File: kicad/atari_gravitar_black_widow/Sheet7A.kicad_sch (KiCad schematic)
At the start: 29 parts

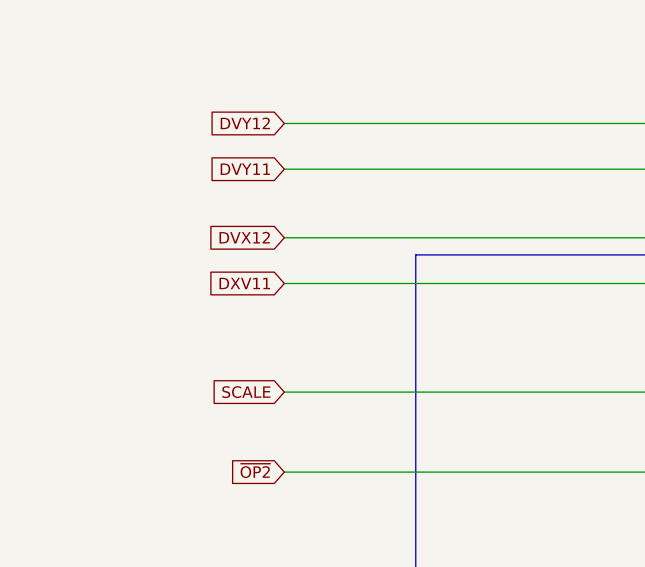
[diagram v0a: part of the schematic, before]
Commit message: Removed more warnings - 25 warnings remain
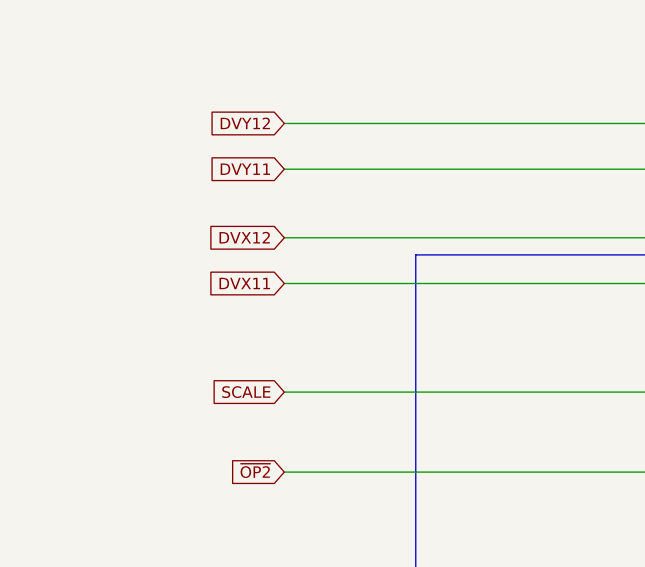
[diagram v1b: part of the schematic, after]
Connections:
- net DXV11 renamed DVX11
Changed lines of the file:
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@@
     )
   )
-  (global_label "DXV11" (shape input) (at 50.165 85.09 180) (fields_autoplaced)
+  (global_label "DVX11" (shape input) (at 50.165 85.09 180) (fields_autoplaced)
     (effects (font (size 1.27 1.27)) (justify right))
-    (property "Intersheet References" "${INTERSHEET_REFS}" (id 0) (at 0 0 0)
-      (effects (font (size 1.27 1.27)) hide)
+    (property "Intersheet References" "${INTERSHEET_REFS}" (id 0) (at 41.8537 85.0106 0)
+      (effects (font (size 1.27 1.27)) (justify right) hide)
     )
   )

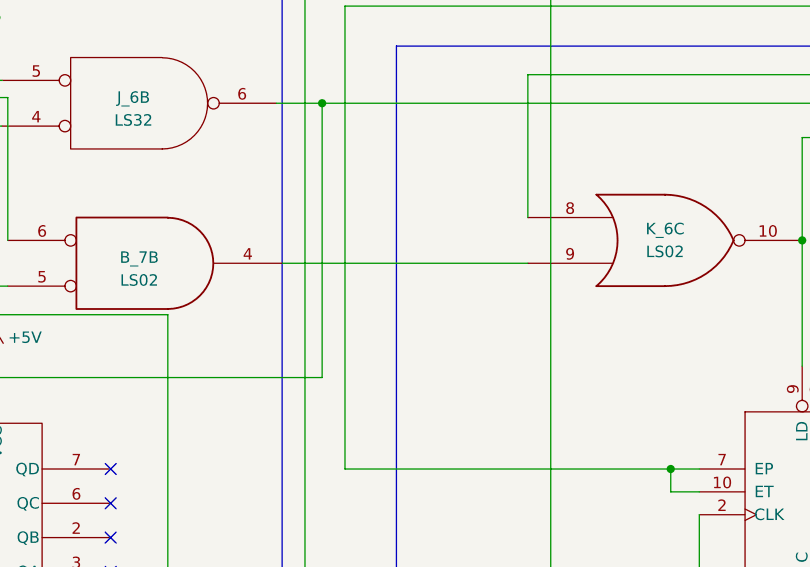
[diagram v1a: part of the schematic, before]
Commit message: 20 warnings left kicad 6.0
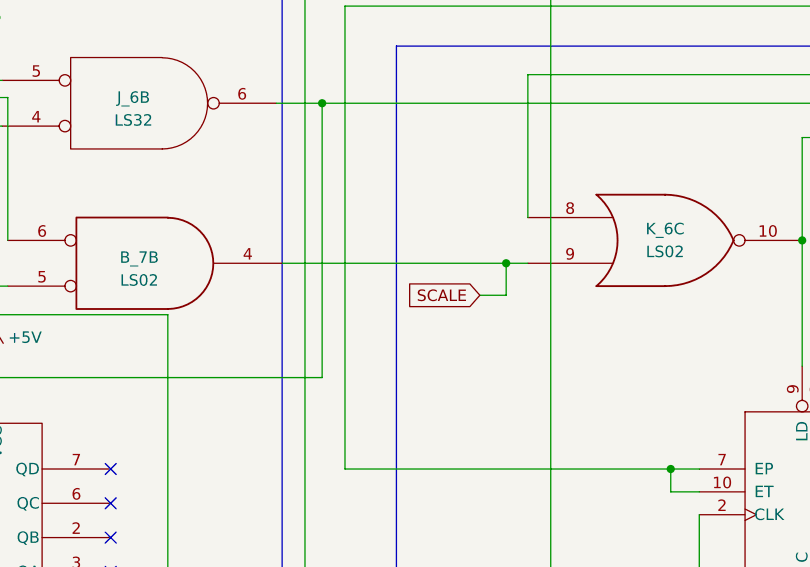
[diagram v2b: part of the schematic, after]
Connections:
- net SCALE: now also B_7.4, K_6.9
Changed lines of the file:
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@@
   (junction (at 361.315 255.905) (diameter 0) (color 0 0 0 0)
+  )
+  (junction (at 179.197 269.875) (diameter 0) (color 0 0 0 0)
   )
   (junction (at 401.32 295.275) (diameter 0) (color 0 0 0 0)
@@
     (stroke (width 0) (type default) (color 0 0 0 0))
   )
+  (wire (pts (xy 179.197 273.431) (xy 176.276 273.431))
+    (stroke (width 0) (type default) (color 0 0 0 0))
+  )
   (polyline (pts (xy 64.77 140.97) (xy 305.435 140.97))
     (stroke (width 0) (type default) (color 0 0 0 0))
@@
     (stroke (width 0) (type default) (color 0 0 0 0))
   )
-  (wire (pts (xy 154.305 269.875) (xy 181.61 269.875))
+  (wire (pts (xy 154.305 269.875) (xy 179.197 269.875))
     (stroke (width 0) (type default) (color 0 0 0 0))
   )
@@
     (stroke (width 0) (type default) (color 0 0 0 0))
   )
+  (wire (pts (xy 179.197 269.875) (xy 179.197 273.431))
+    (stroke (width 0) (type default) (color 0 0 0 0))
+  )
   (wire (pts (xy 361.315 255.905) (xy 361.315 281.305))
     (stroke (width 0) (type default) (color 0 0 0 0))
@@
   )
   (wire (pts (xy 461.645 205.105) (xy 461.645 254.635))
+    (stroke (width 0) (type default) (color 0 0 0 0))
+  )
+  (wire (pts (xy 179.197 269.875) (xy 181.61 269.875))
     (stroke (width 0) (type default) (color 0 0 0 0))
   )
@@
     )
   )
+  (global_label "SCALE" (shape input) (at 176.276 273.431 180) (fields_autoplaced)
+    (effects (font (size 1.27 1.27)) (justify right))
+    (property "Intersheet References" "${INTERSHEET_REFS}" (id 0) (at 168.2066 273.3516 0)
+      (effects (font (size 1.27 1.27)) (justify right) hide)
+    )
+  )

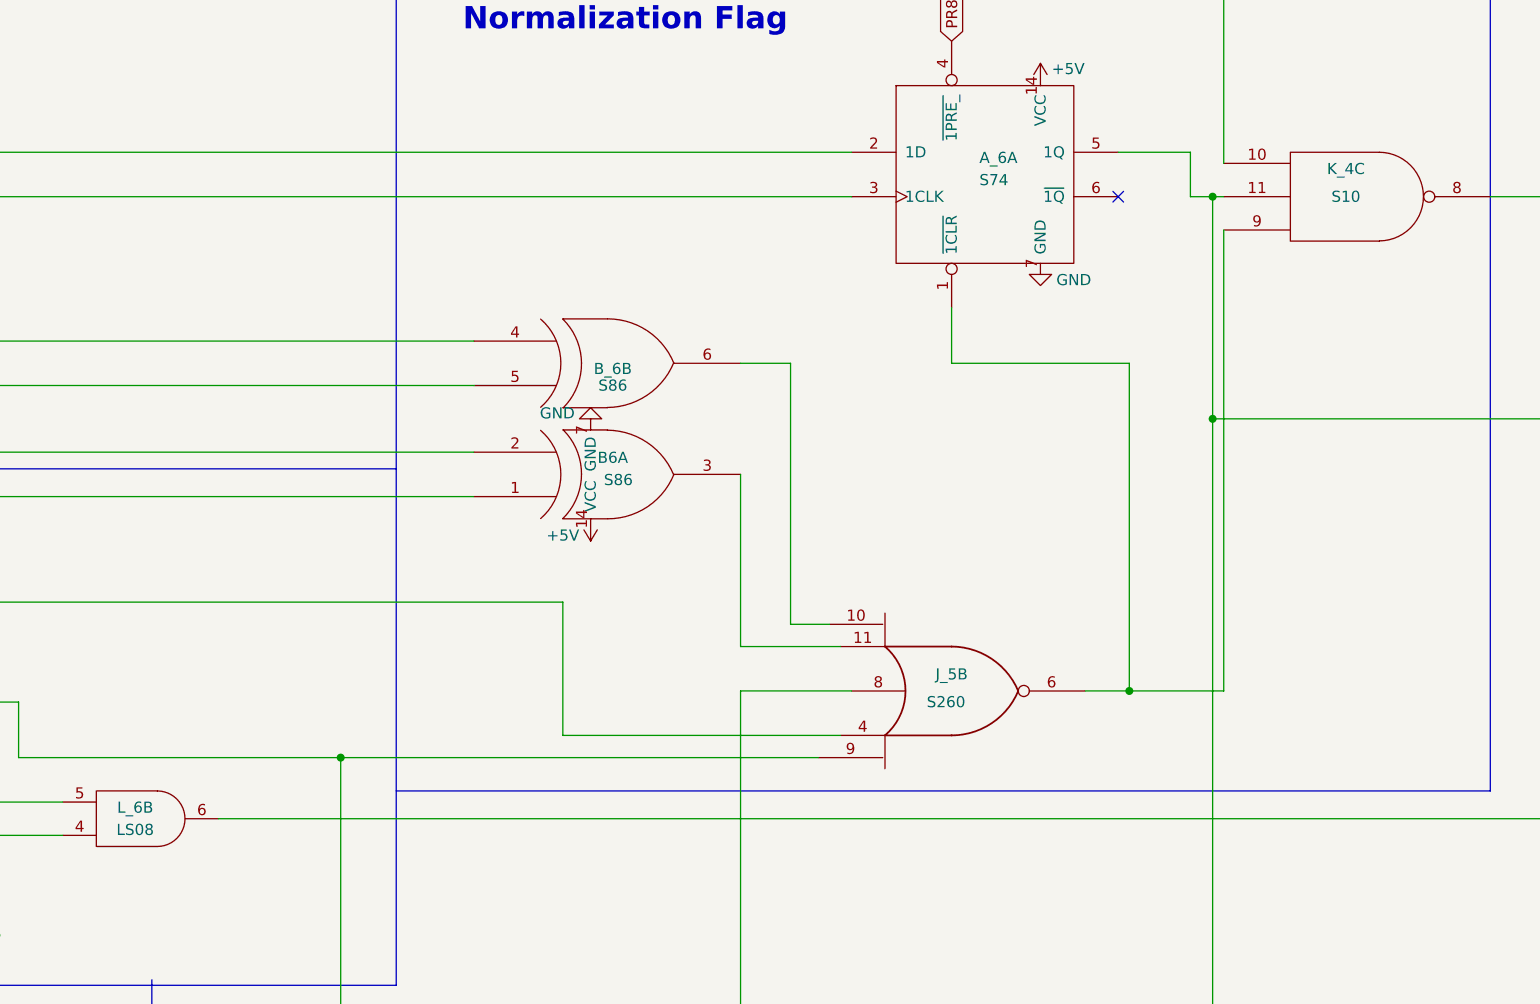
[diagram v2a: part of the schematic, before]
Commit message: Fixed all warnings and errors
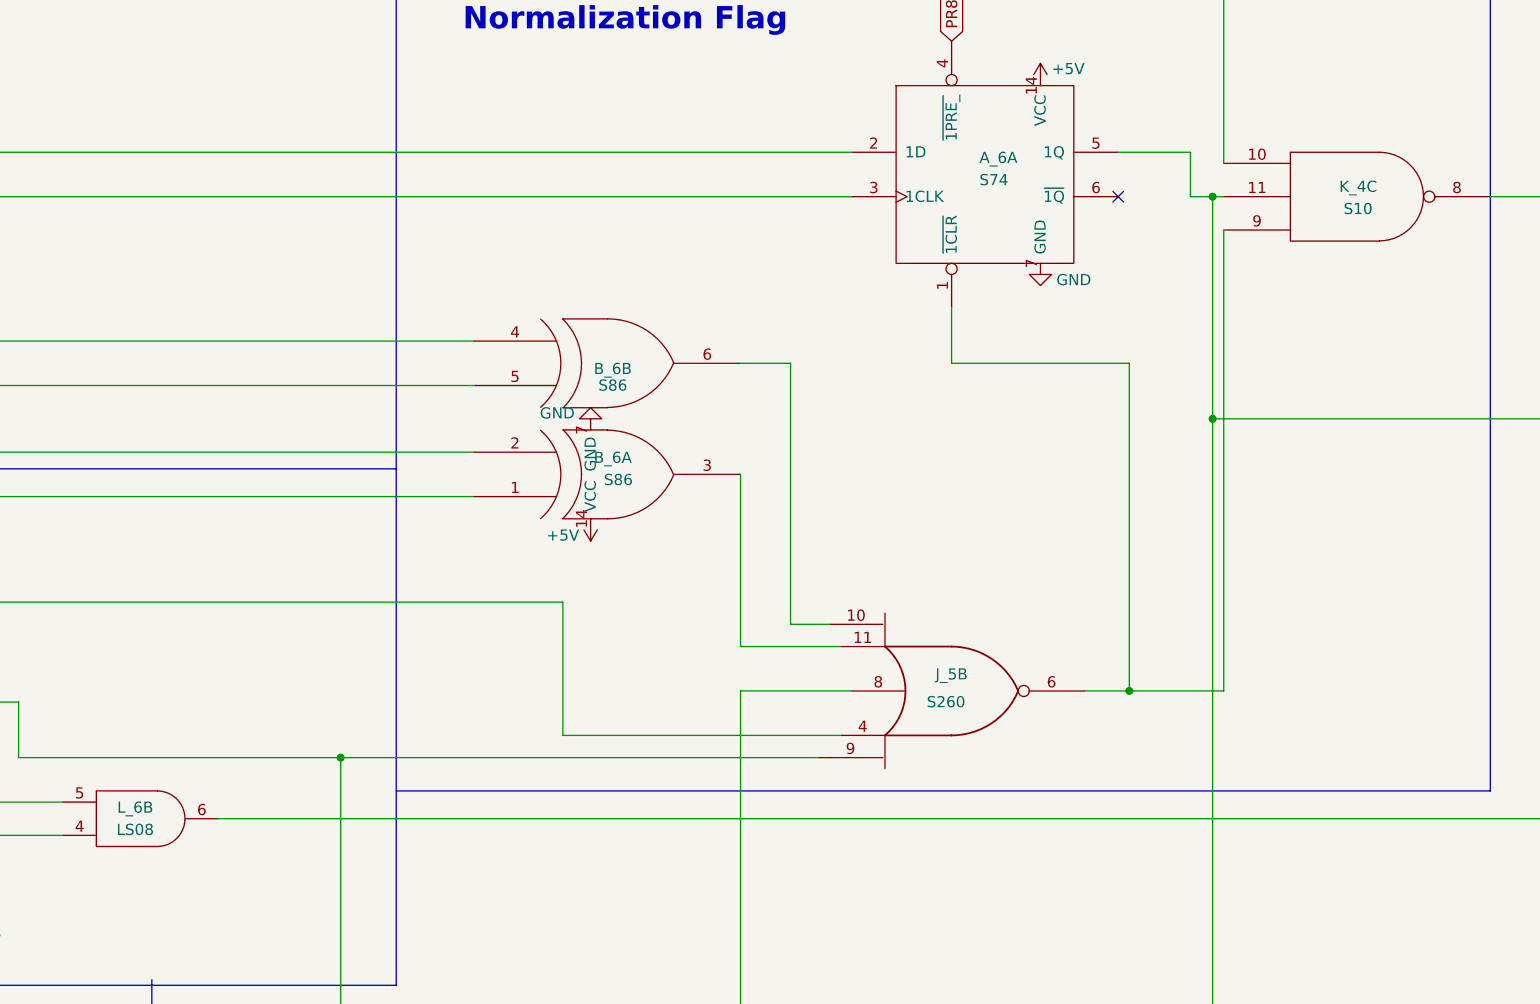
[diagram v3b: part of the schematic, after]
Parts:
- renumbered B6 to B_6
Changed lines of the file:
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@@
     (pin "6")
-  )
-  (symbol (lib_id "atari_grav_bw:LS10") (at 415.29 50.8 0) (unit 3)
-    (in_bom yes) (on_board yes)
-    (property "Reference" "K_4" (id 0) (at 414.02 47.625 0))
-    (property "Value" "S10" (id 1) (at 414.02 50.8 0))
-    (property "Footprint" "" (id 2) (at 415.29 50.8 0)
-      (effects (font (size 1.27 1.27)) hide)
-    )
-    (property "Datasheet" "" (id 3) (at 415.29 50.8 0)
-      (effects (font (size 1.27 1.27)) hide)
-    )
-    (pin "10")
-    (pin "11")
-    (pin "8")
-    (pin "9")
   )
   (symbol (lib_id "Star_Wars_Vector_PCB:LS08") (at 275.59 121.92 0) (mirror x) (unit 2)
@@
   (symbol (lib_id "Star_Wars_Vector_PCB:LS86") (at 329.565 82.55 0) (mirror x) (unit 1)
     (in_bom yes) (on_board yes)
-    (property "Reference" "B6" (id 0) (at 330.2 80.645 0))
+    (property "Reference" "B_6" (id 0) (at 330.2 80.645 0))
     (property "Value" "S86" (id 1) (at 330.835 83.185 0))
     (property "Footprint" "" (id 2) (at 329.565 82.55 0)
@@
     (pin "1")
   )
+  (symbol (lib_id "atari_grav_bw:LS10") (at 415.29 50.8 0) (unit 3)
+    (in_bom yes) (on_board yes)
+    (property "Reference" "K_4" (id 0) (at 415.417 49.657 0))
+    (property "Value" "S10" (id 1) (at 415.417 52.197 0))
+    (property "Footprint" "" (id 2) (at 415.29 50.8 0)
+      (effects (font (size 1.27 1.27)) hide)
+    )
+    (property "Datasheet" "" (id 3) (at 415.29 50.8 0)
+      (effects (font (size 1.27 1.27)) hide)
+    )
+    (pin "10")
+    (pin "11")
+    (pin "8")
+    (pin "9")
+  )
   (symbol (lib_id "power:+5V") (at 234.315 156.21 0) (unit 1)

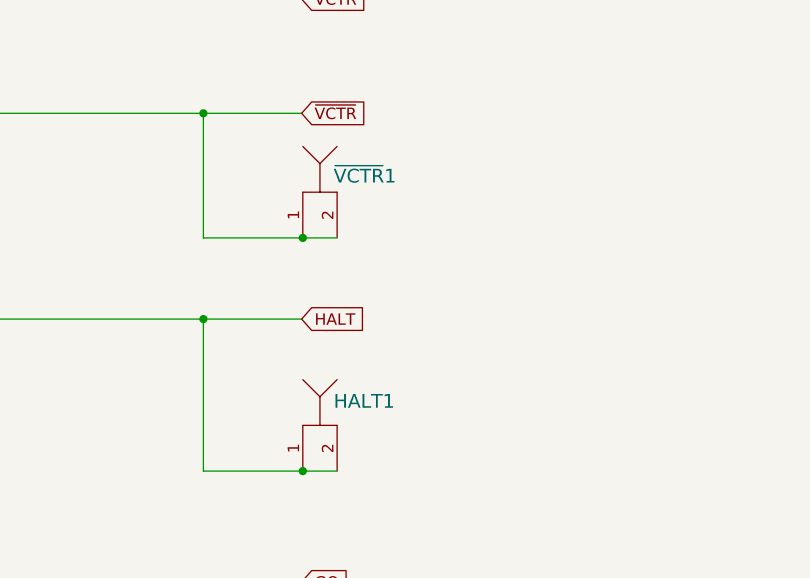
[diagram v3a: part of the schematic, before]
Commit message: Added PCB outline
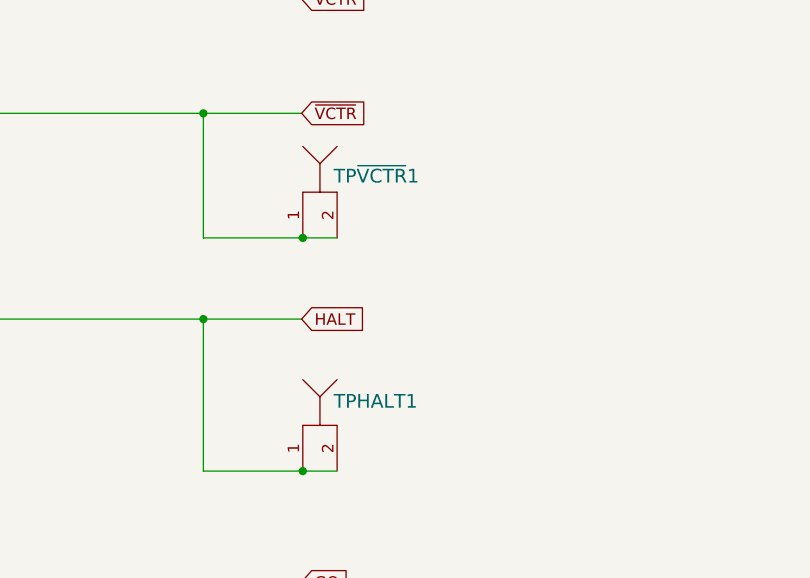
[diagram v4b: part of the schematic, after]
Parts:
- renumbered HALT1 to TPHALT1, ~{VCTR}1 to TP~{VCTR}1
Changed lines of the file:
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@@
   (symbol (lib_id "atari_grav_bw:TP") (at 518.287 207.391 0) (unit 1)
     (in_bom yes) (on_board yes)
-    (property "Reference" "HALT1" (id 0) (at 519.811 204.724 0)
+    (property "Reference" "TPHALT1" (id 0) (at 519.811 204.724 0)
       (effects (font (size 1.524 1.524)) (justify left))
     )
@@
   (symbol (lib_id "atari_grav_bw:TP") (at 518.287 181.483 0) (unit 1)
     (in_bom yes) (on_board yes)
-    (property "Reference" "~{VCTR}1" (id 0) (at 519.811 179.705 0)
+    (property "Reference" "TP~{VCTR}1" (id 0) (at 519.811 179.705 0)
       (effects (font (size 1.524 1.524)) (justify left))
     )

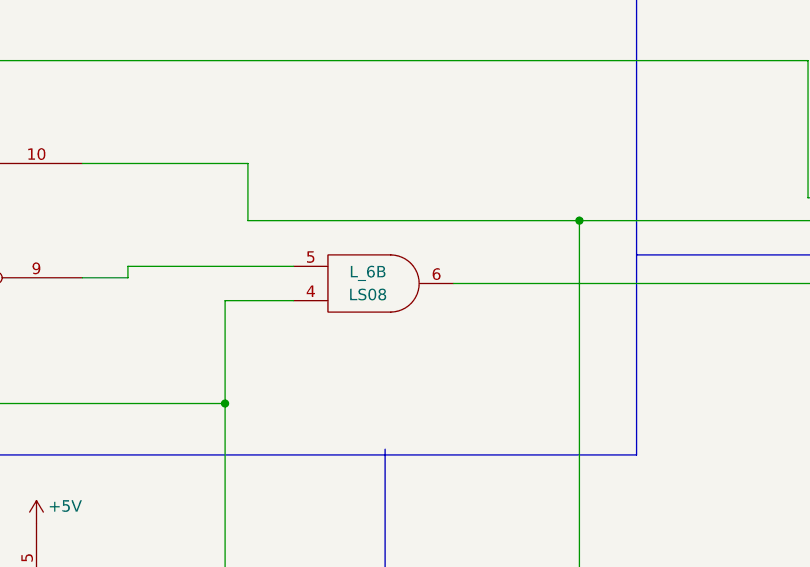
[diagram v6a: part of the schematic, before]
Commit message: place ttl
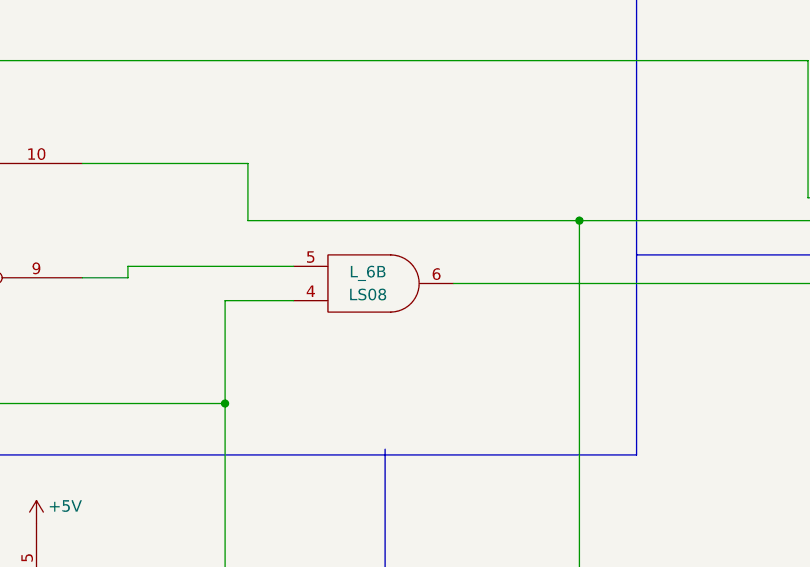
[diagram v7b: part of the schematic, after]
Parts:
- A_6, B_6, B_7: footprint (none) -> Star_Wars_Vector_PCB:DIP14
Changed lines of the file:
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@@
     (property "Reference" "B_6" (id 0) (at 330.2 70.485 0))
     (property "Value" "S86" (id 1) (at 330.2 72.39 0))
-    (property "Footprint" "" (id 2) (at 329.565 69.85 0)
+    (property "Footprint" "Star_Wars_Vector_PCB:DIP14" (id 2) (at 329.565 69.85 0)
       (effects (font (size 1.27 1.27)) hide)
     )
@@
     (property "Reference" "B_6" (id 0) (at 330.2 80.645 0))
     (property "Value" "S86" (id 1) (at 330.835 83.185 0))
-    (property "Footprint" "" (id 2) (at 329.565 82.55 0)
+    (property "Footprint" "Star_Wars_Vector_PCB:DIP14" (id 2) (at 329.565 82.55 0)
       (effects (font (size 1.27 1.27)) hide)
     )
@@
       (effects (font (size 1.27 1.27)) (justify left))
     )
-    (property "Footprint" "" (id 2) (at 373.38 54.61 0)
+    (property "Footprint" "Star_Wars_Vector_PCB:DIP14" (id 2) (at 373.38 54.61 0)
       (effects (font (size 7.62 7.62)) hide)
     )
@@
     (property "Reference" "B_7" (id 0) (at 138.43 269.24 0))
     (property "Value" "LS02" (id 1) (at 138.43 271.78 0))
-    (property "Footprint" "" (id 2) (at 139.065 269.875 0)
+    (property "Footprint" "Star_Wars_Vector_PCB:DIP14" (id 2) (at 139.065 269.875 0)
       (effects (font (size 1.27 1.27)) hide)
     )
@@
       (effects (font (size 1.27 1.27)) (justify left))
     )
-    (property "Footprint" "" (id 2) (at 99.695 224.155 0)
-      (effects (font (size 1.27 1.27)) hide)
-    )
+    (property "Footprint" "Star_Wars_Vector_PCB:DIP14" (id 2) (at 99.695 224.155 0)
+      (effects (font (size 1.27 1.27)) hide)
+    )
